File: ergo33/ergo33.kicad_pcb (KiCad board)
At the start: 2 copper layers, 168.9 x 117 mm, 114 parts, among them SW1 SW_Push, SW46 Rotary_Encoder_Switch, U1 ATmega32U4-AU, Y1 16MHz

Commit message: Fix DRC errors
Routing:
- net GND: track 172.0 -> 174.6 mm, vias 29 -> 30
- net Net-(JP2-Pad1): track 15.8 -> 16.4 mm
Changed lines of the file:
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@@
     (thickness 1.6)
     (drawings 18)
-    (tracks 951)
+    (tracks 953)
     (zones 0)
     (modules 114)
@@
     (add_net "Net-(R5-Pad2)")
     (add_net "Net-(R6-Pad2)")
-    (add_net "Net-(U1-Pad1)")
-    (add_net "Net-(U1-Pad10)")
-    (add_net "Net-(U1-Pad11)")
-    (add_net "Net-(U1-Pad12)")
-    (add_net "Net-(U1-Pad18)")
-    (add_net "Net-(U1-Pad19)")
-    (add_net "Net-(U1-Pad20)")
-    (add_net "Net-(U1-Pad26)")
-    (add_net "Net-(U1-Pad42)")
-    (add_net "Net-(U1-Pad8)")
-    (add_net "Net-(U1-Pad9)")
-    (add_net "Net-(USB1-Pad10)")
-    (add_net "Net-(USB1-Pad11)")
-    (add_net "Net-(USB1-Pad14)")
-    (add_net "Net-(USB1-Pad15)")
-    (add_net "Net-(USB1-Pad2)")
-    (add_net "Net-(USB1-Pad20)")
-    (add_net "Net-(USB1-Pad22)")
-    (add_net "Net-(USB1-Pad23)")
-    (add_net "Net-(USB1-Pad3)")
-    (add_net "Net-(USB1-Pad8)")
-    (add_net "Net-(USB2-Pad2)")
     (add_net ROW0)
     (add_net ROW1)
@@
   (via (at 180.1 80.9) (size 0.8) (drill 0.4) (layers F.Cu B.Cu) (net 2))
   (segment (start 177.46 80.9) (end 180.1 80.9) (width 0.375) (layer B.Cu) (net 2))
+  (via (at 179.8 37) (size 0.8) (drill 0.4) (layers F.Cu B.Cu) (net 2))
+  (segment (start 179.8 34.4) (end 179.8 37) (width 0.375) (layer B.Cu) (net 2))
   (segment (start 185.5625 63.332459) (end 186.670953 64.440912) (width 0.25) (layer B.Cu) (net 3))
   (segment (start 185.5625 61.4) (end 185.5625 63.332459) (width 0.25) (layer B.Cu) (net 3))
@@
   (segment (start 161.9 82.7) (end 167.7 82.7) (width 0.25) (layer B.Cu) (net 45))
   (segment (start 161.4 83.2) (end 161.9 82.7) (width 0.25) (layer B.Cu) (net 45))
-  (segment (start 173.15 46.9) (end 175.7 46.9) (width 0.25) (layer B.Cu) (net 46))
   (segment (start 177.4 45.2) (end 177.4 34.4) (width 0.25) (layer B.Cu) (net 46))
   (segment (start 175.7 46.9) (end 177.4 45.2) (width 0.25) (layer B.Cu) (net 46))
+  (segment (start 175.7 46.9) (end 172.55 46.9) (width 0.25) (layer B.Cu) (net 46))
   (segment (start 167.129194 35.277544) (end 167.129194 35.429194) (width 0.25) (layer F.Cu) (net 47))
   (segment (start 167.129194 35.277544) (end 167.129194 35.629194) (width 0.25) (layer F.Cu) (net 47))

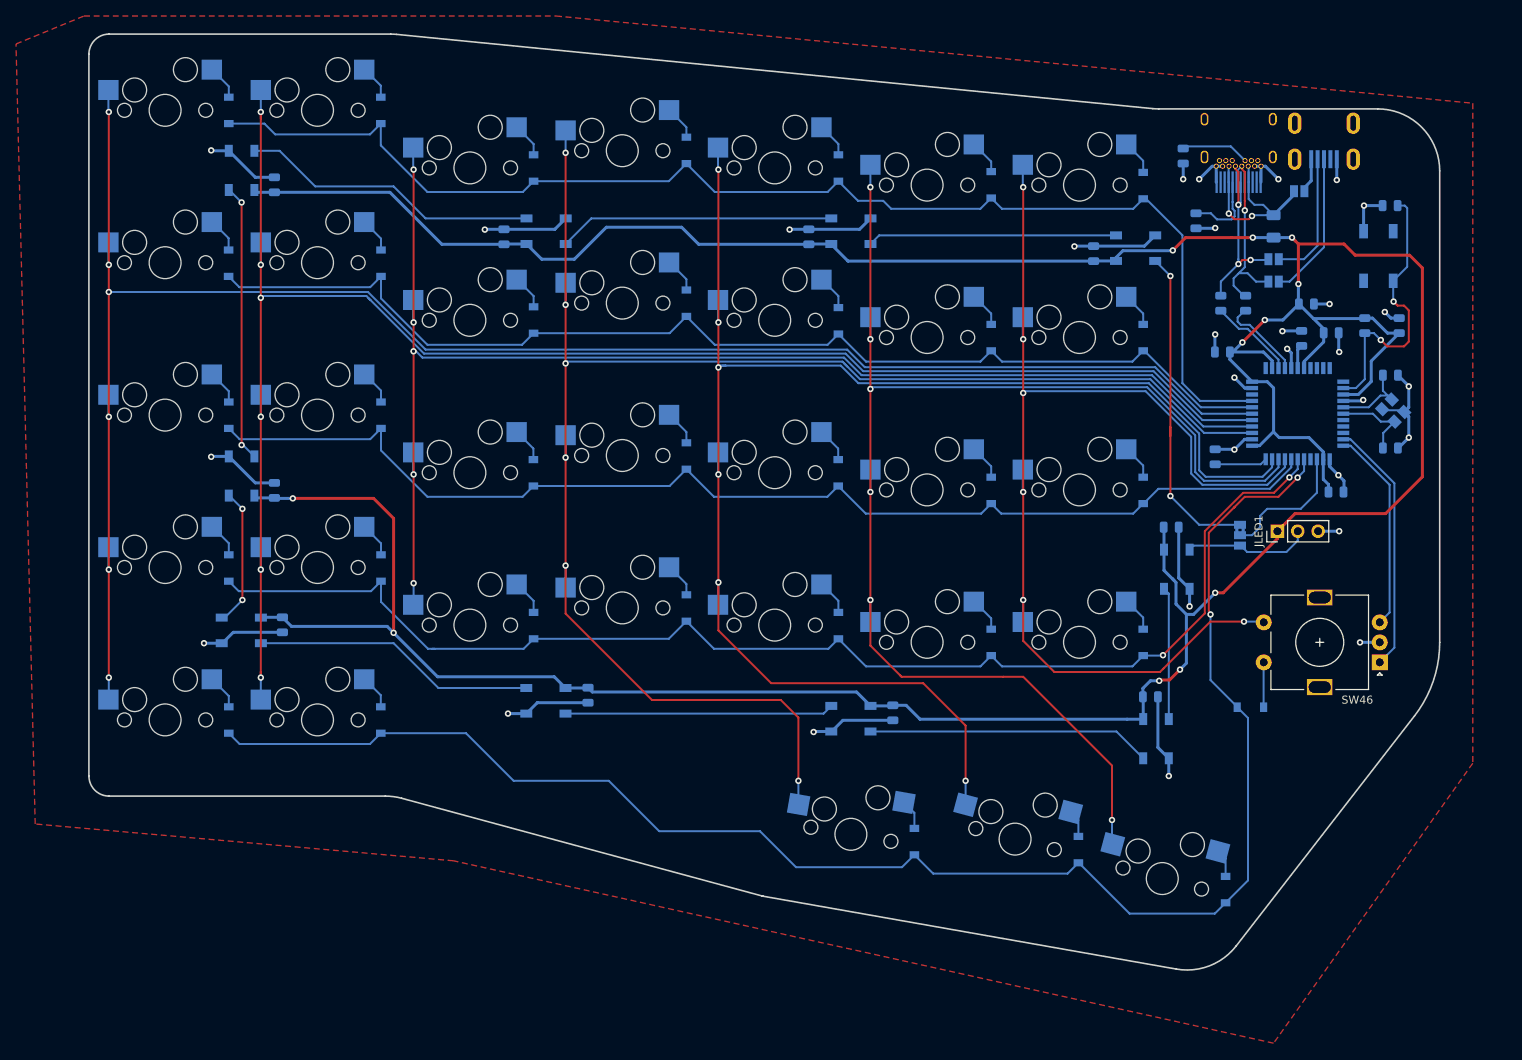
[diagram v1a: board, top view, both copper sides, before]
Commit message: ergo33: Change USB connectors and add ESD protection
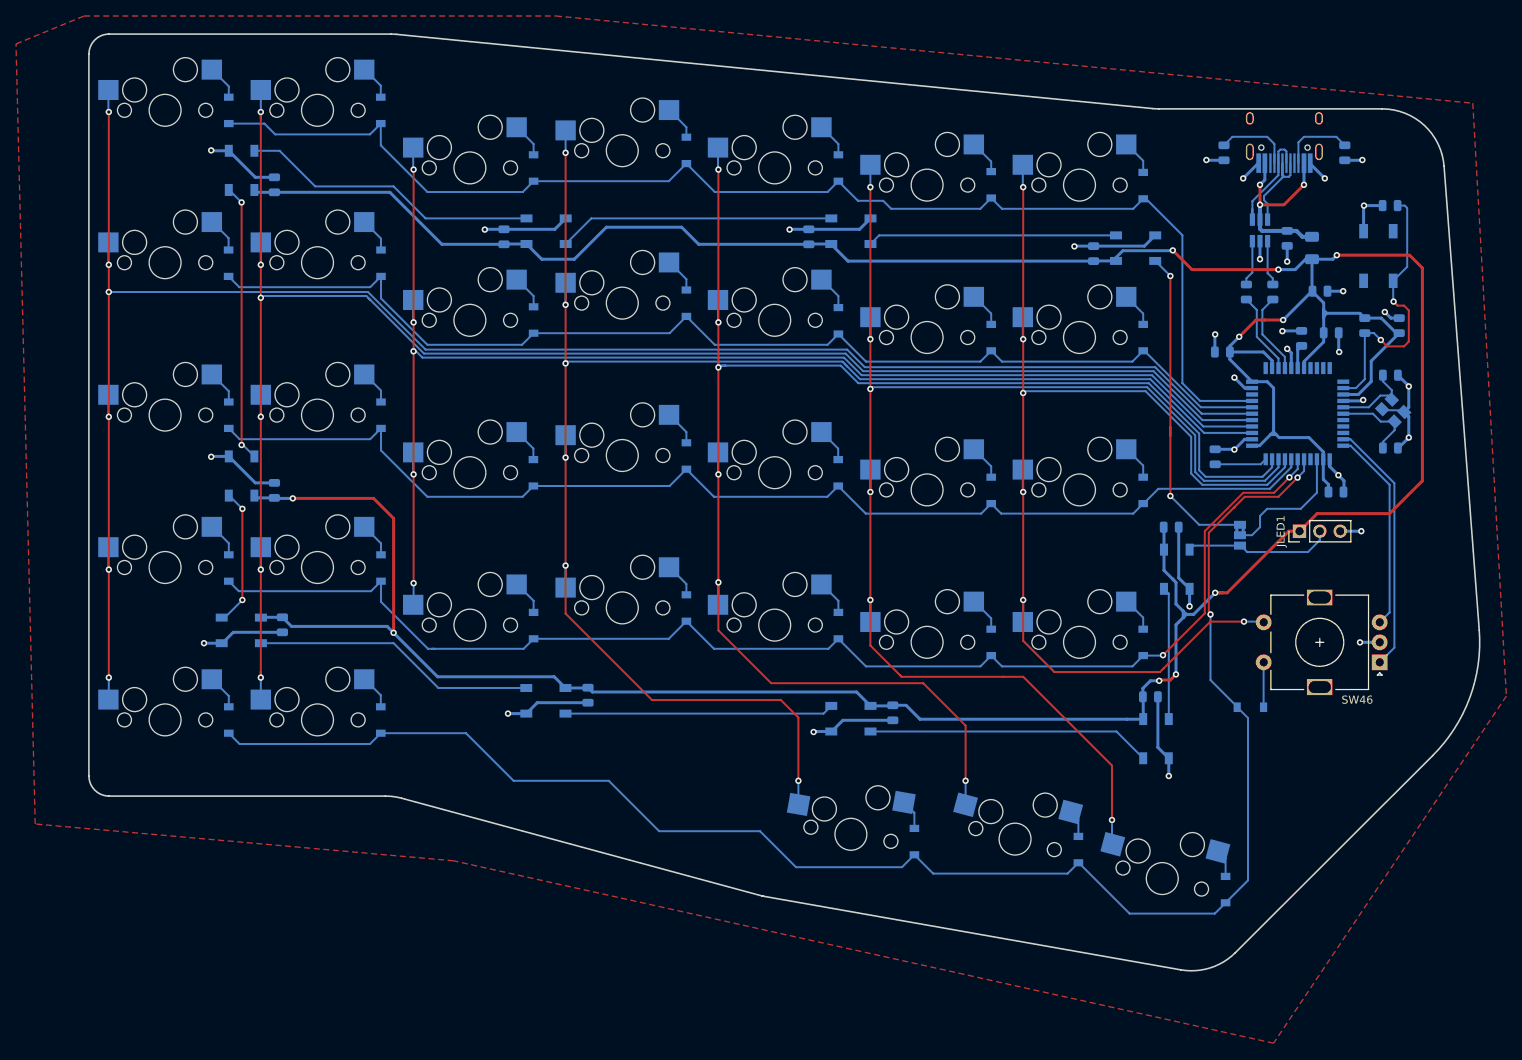
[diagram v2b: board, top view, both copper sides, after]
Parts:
- removed JP2, JP3, JP4: SolderJumper_2_Open, Jumper:SolderJumper-2_P1.3mm_Open_Pad1.0x1.5mm
- removed USB2: Molex-0548190589, random-keyboard-parts:Molex-0548190589
- added C20: 0.1uF, Capacitor_SMD:C_0805_2012Metric, B.Cu at (173.6, 44.3)
- added U2: USBLC6-2SC6, Package_TO_SOT_SMD:SOT-23-6_Handsoldering, B.Cu at (170.2, 43.3)
- USB1: value Wurth-632723300011 -> HRO-TYPE-C-31-M-12; footprint Type-C:Wurth-632723300011-HandSoldering -> Type-C:HRO-TYPE-C-31-M-12-HandSoldering
- moved R6 20.2 mm to (180.8, 33.6)
- moved R5 9.19 mm to (165.7, 33.6)
- moved USB1 5.78 mm to (173.3, 26.7)
- moved F1 5.51 mm to (176.7, 45.5)
- moved R3 3.68 mm to (171.8, 51.0)
- moved R2 3.49 mm to (168.5, 51.0)
- moved JLED1 2.76 mm to (175.1, 80.9)
- moved C7 2.33 mm to (177.7, 50.9)
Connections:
- net Net-(R2-Pad1) renamed RD-
- net Net-(R3-Pad1) renamed RD+
- F1 pad 1: PWR_IN -> VBUS
- USB1 pad 10: (no net) -> Net-(R6-Pad2)
- USB1 pad 11: (no net) -> VBUS
- USB1 pad 2: (no net) -> VBUS
- USB1 pad 4: PWR_IN -> Net-(R5-Pad2)
- USB1 pad 5: Net-(R5-Pad2) -> DBUS-
- USB1 pad 6: D+ -> DBUS+
- USB1 pad 7: D- -> DBUS-
- USB1 pad 8: (no net) -> DBUS+
- USB1 pad 9: PWR_IN -> (no net)
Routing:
- net PWR_IN: track 25.4 -> 0.00 mm, vias 2 -> 0
- net VBUS: track 0.00 -> 24.8 mm, vias 0 -> 3
- net D-: track 24.3 -> 5.89 mm, vias 3 -> 0
- net Net-(JP3-Pad1): track 18.4 -> 0.00 mm
- net D+: track 22.7 -> 5.94 mm, vias 1 -> 0
- net Net-(JP2-Pad1): track 16.4 -> 0.00 mm
- net DBUS-: track 0.00 -> 13.8 mm
- net DBUS+: track 0.00 -> 12.4 mm
- net GND: track 174.6 -> 170.2 mm, vias 30 -> 31
- net Net-(JP4-Pad1): track 4.35 -> 0.00 mm
- net +5V: track 487.0 -> 490.7 mm, vias 11 -> 10
- net LEDS2: track 15.8 -> 19.4 mm
- net RD-: track 10.8 -> 10.2 mm
- net Net-(R6-Pad2): track 8.57 -> 9.12 mm
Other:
- board size 168.9 x 117 mm -> 173.8 x 117.1 mm
- net class C data removed
- net class Power in removed

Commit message: Add mounting holes and tweak silkscreen
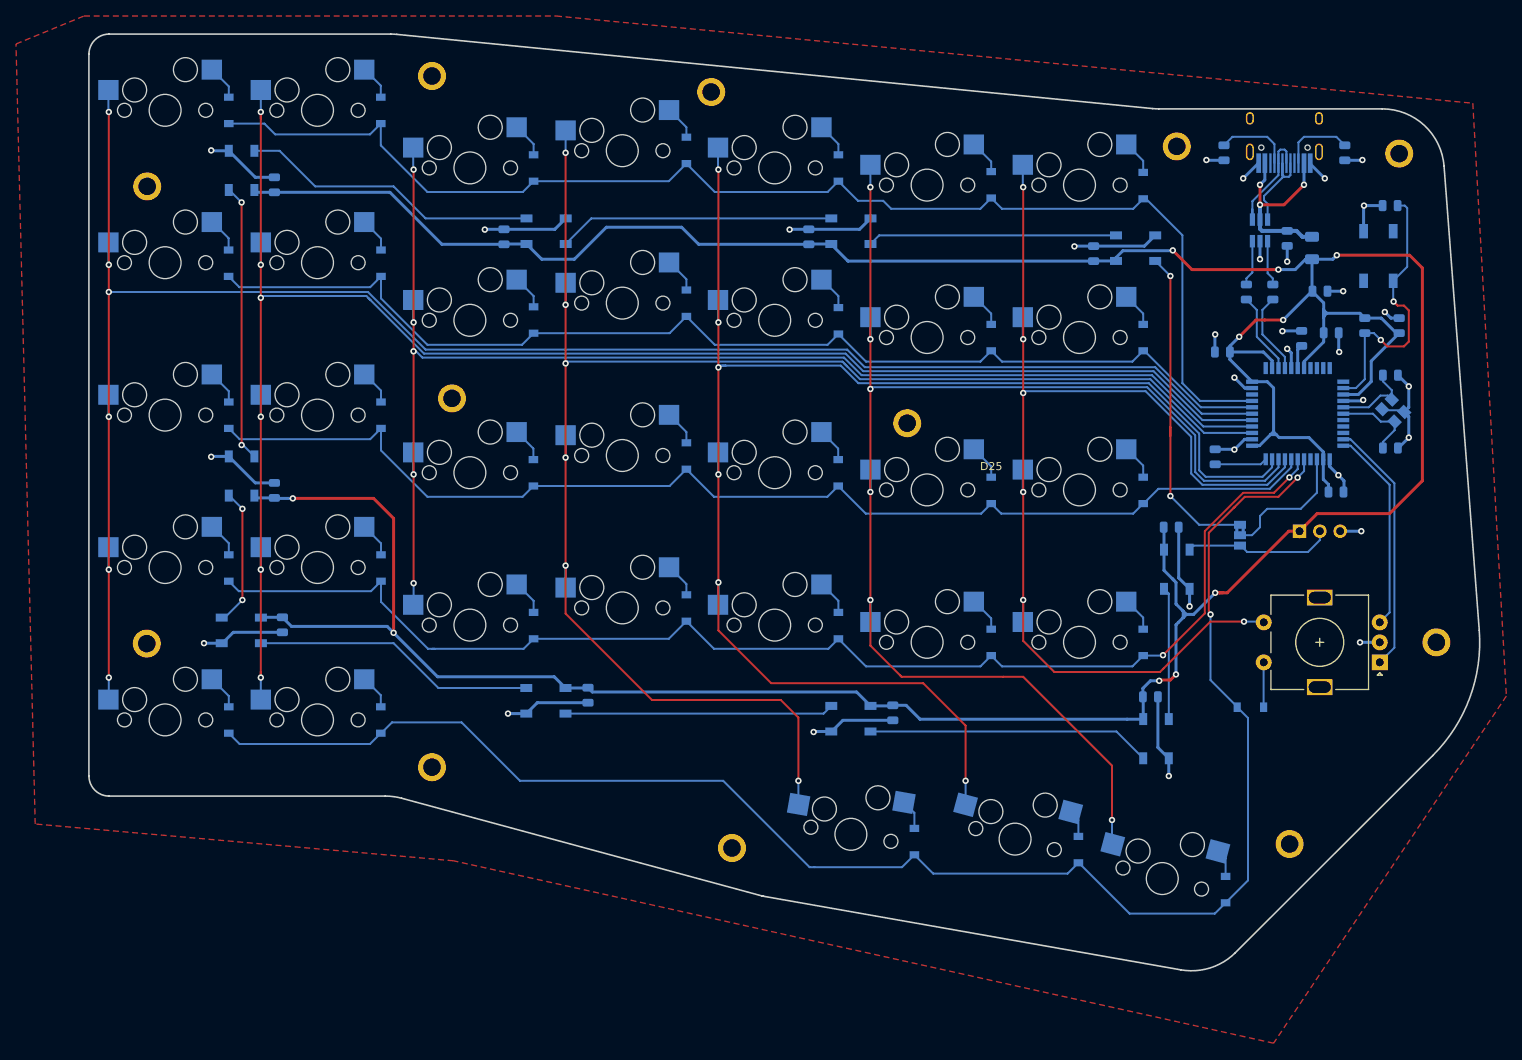
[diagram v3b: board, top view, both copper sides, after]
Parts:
- removed SW1: SW_Push, random-keyboard-parts:SKQG-1155865
- added REF**: MountingHole_2.2mm_M2_ISO7380_Pad_Courtyard, tunks-parts:MountingHole_2.2mm_M2_ISO7380_Pad_Courtyard, F.Cu at (159.8, 32.8)
- added REF**: MountingHole_2.2mm_M2_ISO7380_Pad_Courtyard, tunks-parts:MountingHole_2.2mm_M2_ISO7380_Pad_Courtyard, F.Cu at (173.9, 120.0)
- added REF**: MountingHole_2.2mm_M2_ISO7380_Pad_Courtyard, tunks-parts:MountingHole_2.2mm_M2_ISO7380_Pad_Courtyard, F.Cu at (192.2, 94.8)
- added REF**: MountingHole_2.2mm_M2_ISO7380_Pad_Courtyard, tunks-parts:MountingHole_2.2mm_M2_ISO7380_Pad_Courtyard, F.Cu at (187.6, 33.7)
- added REF**: MountingHole_2.2mm_M2_ISO7380_Pad_Courtyard, tunks-parts:MountingHole_2.2mm_M2_ISO7380_Pad_Courtyard, F.Cu at (126.1, 67.4)
- added REF**: MountingHole_2.2mm_M2_ISO7380_Pad_Courtyard, tunks-parts:MountingHole_2.2mm_M2_ISO7380_Pad_Courtyard, F.Cu at (101.6, 26.0)
- added REF**: MountingHole_2.2mm_M2_ISO7380_Pad_Courtyard, tunks-parts:MountingHole_2.2mm_M2_ISO7380_Pad_Courtyard, F.Cu at (66.7, 24.0)
- added REF**: MountingHole_2.2mm_M2_ISO7380_Pad_Courtyard, tunks-parts:MountingHole_2.2mm_M2_ISO7380_Pad_Courtyard, F.Cu at (69.2, 64.3)
- added REF**: MountingHole_2.2mm_M2_ISO7380_Pad_Courtyard, tunks-parts:MountingHole_2.2mm_M2_ISO7380_Pad_Courtyard, F.Cu at (31.1, 37.8)
- added REF**: MountingHole_2.2mm_M2_ISO7380_Pad_Courtyard, tunks-parts:MountingHole_2.2mm_M2_ISO7380_Pad_Courtyard, F.Cu at (31.1, 95.0)
- added REF**: MountingHole_2.2mm_M2_ISO7380_Pad_Courtyard, tunks-parts:MountingHole_2.2mm_M2_ISO7380_Pad_Courtyard, F.Cu at (66.7, 110.4)
- added REF**: MountingHole_2.2mm_M2_ISO7380_Pad_Courtyard, tunks-parts:MountingHole_2.2mm_M2_ISO7380_Pad_Courtyard, F.Cu at (104.2, 120.5)
- added RST: SW_Push, random-keyboard-parts:SKQG-1155865, B.Cu at (185.0, 46.5)
- JLED1: moved to B.Cu
- turned JLED1 to 270 degrees
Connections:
- U1 pad 1: (no net) -> Net-(U1-Pad1)
- U1 pad 10: (no net) -> Net-(U1-Pad10)
- U1 pad 11: (no net) -> Net-(U1-Pad11)
- U1 pad 12: (no net) -> Net-(U1-Pad12)
- U1 pad 18: (no net) -> Net-(U1-Pad18)
- U1 pad 19: (no net) -> Net-(U1-Pad19)
- U1 pad 20: (no net) -> Net-(U1-Pad20)
- U1 pad 26: (no net) -> Net-(U1-Pad26)
- U1 pad 42: (no net) -> Net-(U1-Pad42)
- U1 pad 8: (no net) -> Net-(U1-Pad8)
- U1 pad 9: (no net) -> Net-(U1-Pad9)
- USB1 pad 3: (no net) -> Net-(USB1-Pad3)
- USB1 pad 9: (no net) -> Net-(USB1-Pad9)
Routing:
- net ROW4: track 204.3 -> 205.4 mm

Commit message: ergo33: footprint changes
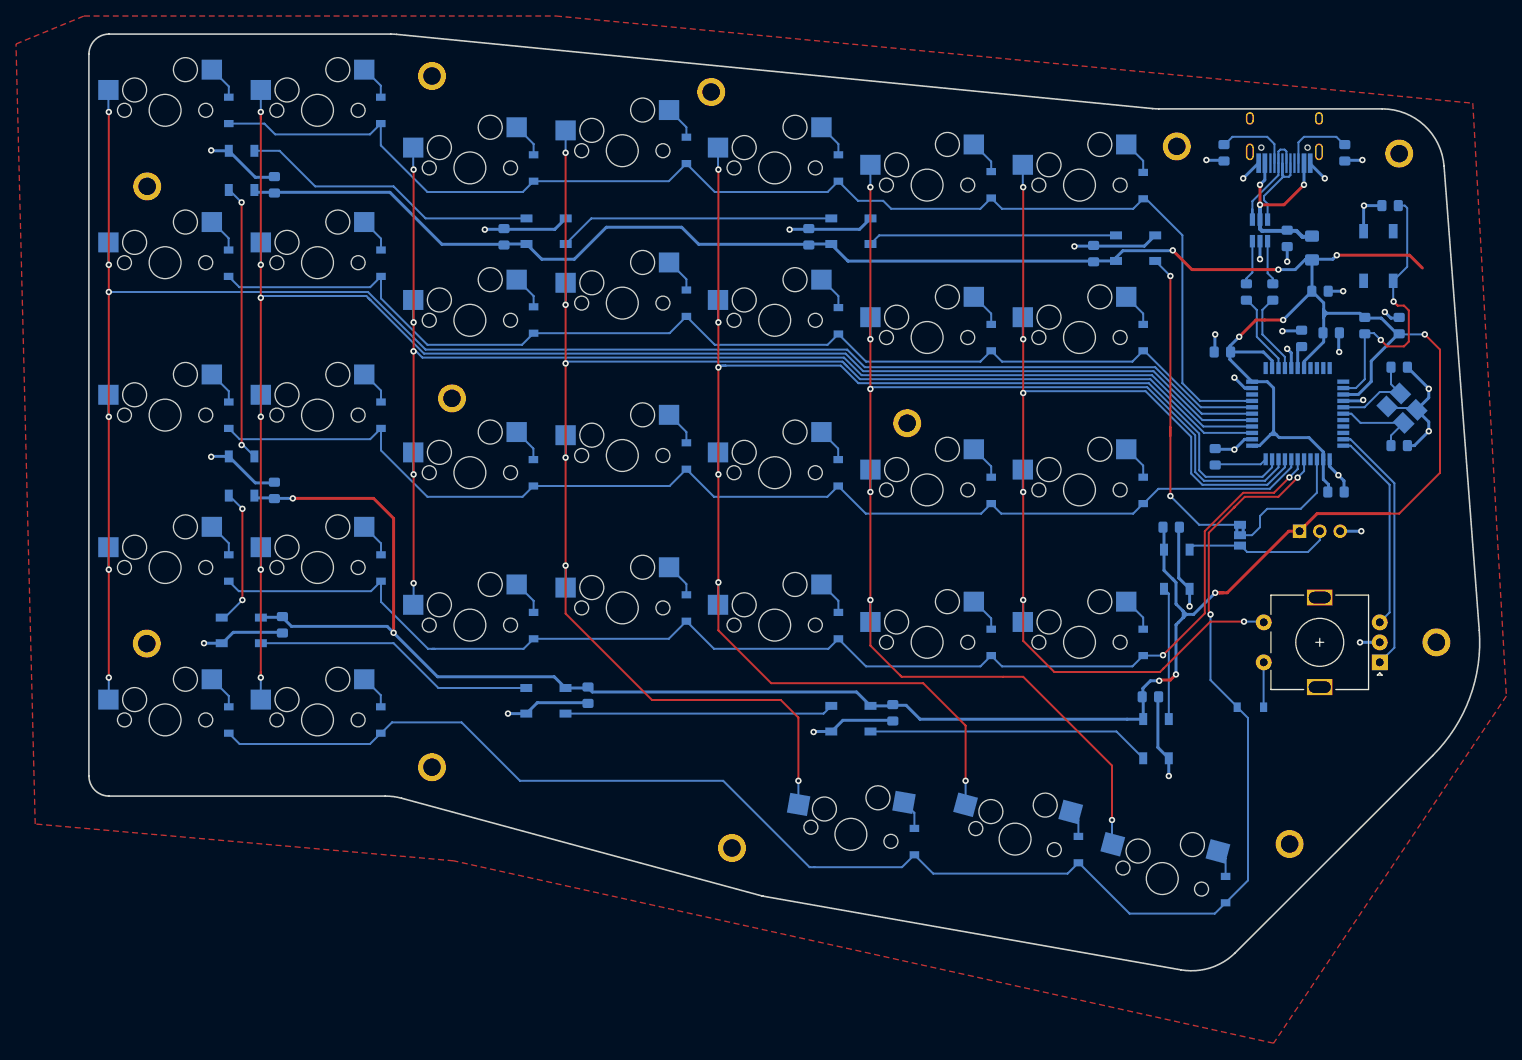
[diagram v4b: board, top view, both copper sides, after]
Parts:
- C1, C10, C11, C12, C13, C14, C15, C16, C17, C18, C19, C2, C20, C3, C4, C5, C6, C7, C8, C9: footprint Capacitor_SMD:C_0805_2012Metric -> Capacitor_SMD:C_0805_2012Metric_Pad1.15x1.40mm_HandSolder
- F1: footprint Fuse:Fuse_1206_3216Metric -> Fuse:Fuse_1206_3216Metric_Pad1.42x1.75mm_HandSolder
- R1, R2, R3, R4, R5, R6: footprint Resistor_SMD:R_0805_2012Metric -> Resistor_SMD:R_0805_2012Metric_Pad1.15x1.40mm_HandSolder
- Y1: footprint Crystal:Crystal_SMD_3225-4Pin_3.2x2.5mm -> Crystal:Crystal_SMD_3225-4Pin_3.2x2.5mm_HandSoldering
- moved C2 1.49 mm to (187.6, 60.4)
- moved Y1 1.14 mm to (187.9, 65.5)
- moved C1 1.14 mm to (187.6, 70.2)
- renumbered RST to SW1
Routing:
- net GND: track 170.2 -> 174.1 mm
- net +5V: track 490.7 -> 488.0 mm, vias 10 -> 11
- net Net-(C2-Pad2): track 10.4 -> 12.8 mm
- net Net-(C1-Pad2): track 10.8 -> 11.6 mm
